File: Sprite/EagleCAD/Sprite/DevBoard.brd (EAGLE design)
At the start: 35 x 35 mm, 29 parts, among them U1 CC430F5137, U2 HMC5883LSMD, U3 ITG-3200, X1 26 MHz

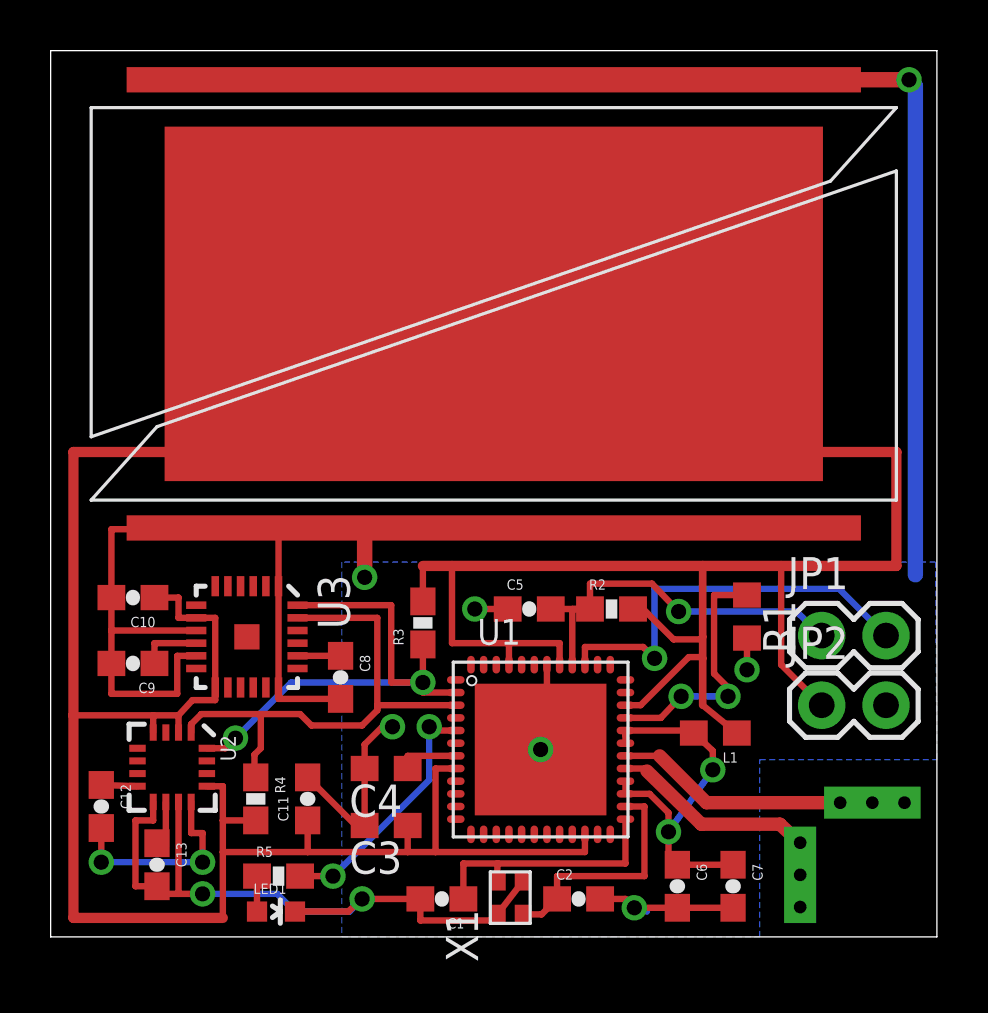
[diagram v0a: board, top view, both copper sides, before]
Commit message: Added header to dev board to disconnect solar cells
Added a header to connect/disconnect the solar cells from VCC to allow
programming with the TI launchpad
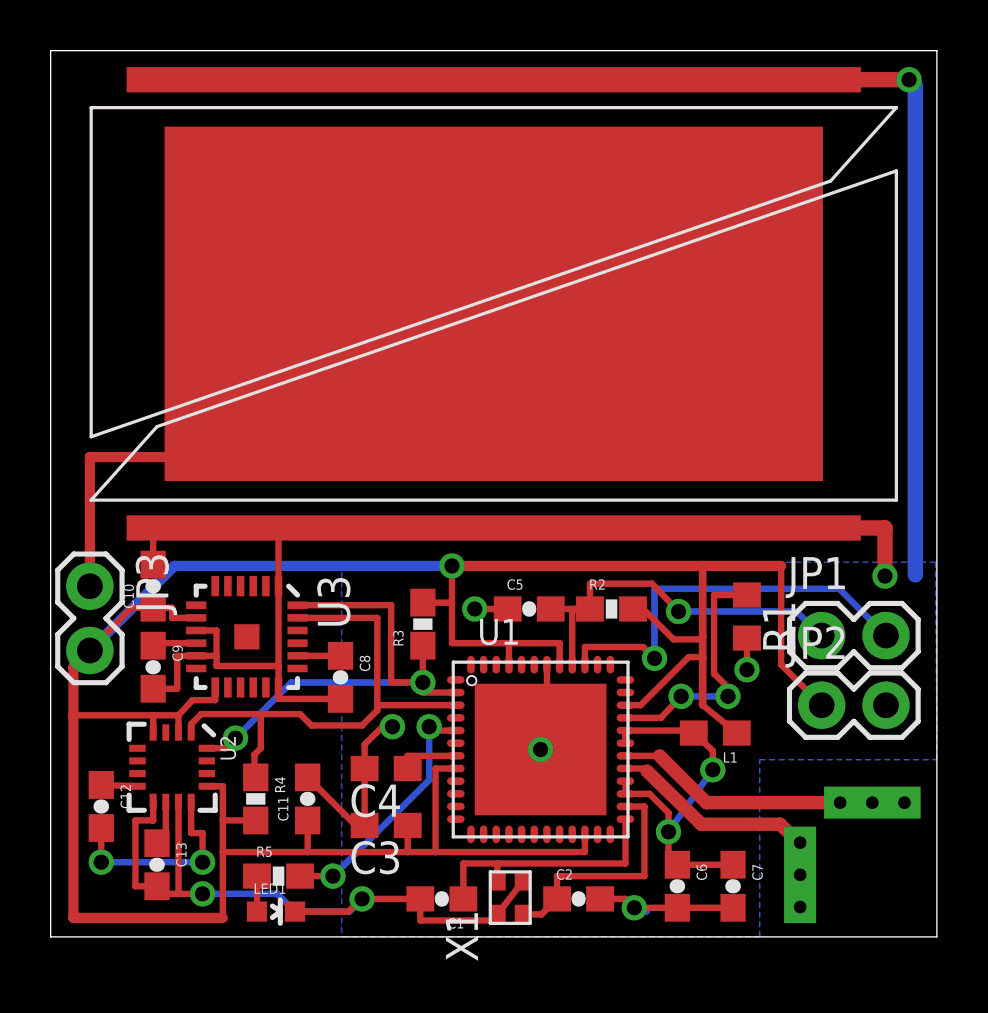
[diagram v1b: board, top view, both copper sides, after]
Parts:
- added JP3: (no value), SparkFun:1X02
- moved C10 0.92 mm to (4.05, 13.8), turned to 90 degrees
- moved C9 0.81 mm to (4.05, 10.7), turned to 270 degrees
- moved R3 0.05 mm to (14.7, 12.3)
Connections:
- new net VSOLAR: JP3.1, S1.PLUS
- net VCC: now also JP3.2; no longer S1.PLUS
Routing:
- net VCC: track 151.6 -> 117.7 mm, vias 0 -> 1
- net VSOLAR: track 0.00 -> 27.1 mm
- net GND: track 130.1 -> 156.3 mm
- net N$9: track 2.45 -> 1.76 mm
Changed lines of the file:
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@@
 <element name="U3" library="SparkFun" package="QFN-24" value="ITG-3200" x="7.75" y="11.85" rot="R270"/>
 <element name="C8" library="SparkFun" package="0603-CAP" value="2.2nF" x="11.45" y="10.25" rot="R270"/>
-<element name="C9" library="SparkFun" package="0603-CAP" value="100nF" x="3.25" y="10.8" rot="R180"/>
-<element name="C10" library="SparkFun" package="0603-CAP" value="10nF" x="3.25" y="13.4" rot="R180"/>
-<element name="R3" library="SparkFun" package="0603-RES" value="4.7K" x="14.7" y="12.4" rot="R90"/>
+<element name="C9" library="SparkFun" package="0603-CAP" value="100nF" x="4.05" y="10.65" rot="R270"/>
+<element name="C10" library="SparkFun" package="0603-CAP" value="10nF" x="4.05" y="13.85" rot="R90"/>
+<element name="R3" library="SparkFun" package="0603-RES" value="4.7K" x="14.7" y="12.35" rot="R90"/>
 <element name="R4" library="SparkFun" package="0603-RES" value="4.7K" x="8.1" y="5.45" rot="R270"/>
 <element name="JP1" library="SparkFun" package="1X02" value="" x="30.45" y="11.9"/>
@@
 <element name="R5" library="SparkFun" package="0603-RES" value="270R" x="9" y="2.4"/>
 <element name="X1" library="ABM11" package="ABM11_CERAMIC-SMD-CRYSTAL" value="26 MHz" x="18.15" y="1.55" rot="R90"/>
+<element name="JP3" library="SparkFun" package="1X02" value="" x="1.55" y="13.85" rot="R270"/>
 </elements>
 <signals>
@@
 <contactref element="R3" pad="2"/>
 <contactref element="R4" pad="2"/>
-<wire x1="33.4" y1="14.65" x2="33.4" y2="19.15" width="0.4064" layer="1"/>
-<wire x1="33.4" y1="19.15" x2="24.8" y2="19.15" width="0.4064" layer="1"/>
-<wire x1="33.4" y1="14.65" x2="28.85" y2="14.65" width="0.4064" layer="1"/>
 <wire x1="28.85" y1="14.65" x2="25.75" y2="14.65" width="0.4064" layer="1"/>
 <wire x1="25.75" y1="14.65" x2="15.85" y2="14.65" width="0.4064" layer="1"/>
-<wire x1="15.85" y1="14.65" x2="14.7" y2="14.65" width="0.4064" layer="1"/>
 <wire x1="0.9" y1="8.75" x2="0.9" y2="0.75" width="0.4064" layer="1"/>
 <wire x1="0.9" y1="0.75" x2="6.8" y2="0.75" width="0.4064" layer="1"/>
@@
 <contactref element="U3" pad="8"/>
 <contactref element="C10" pad="1"/>
-<wire x1="5.75" y1="12.6" x2="5.05" y2="12.6" width="0.254" layer="1"/>
-<wire x1="5.05" y1="12.6" x2="5.05" y2="13.4" width="0.254" layer="1"/>
-<wire x1="5.05" y1="13.4" x2="4.1" y2="13.4" width="0.254" layer="1"/>
-<wire x1="6.5" y1="9.85" x2="6.5" y2="12.6" width="0.254" layer="1"/>
-<wire x1="6.5" y1="12.6" x2="5.75" y2="12.6" width="0.254" layer="1"/>
 <wire x1="6.5" y1="9.35" x2="5.6" y2="9.35" width="0.254" layer="1"/>
 <wire x1="5.6" y1="9.35" x2="5.05" y2="8.75" width="0.254" layer="1"/>
 <contactref element="R2" pad="2"/>
-<wire x1="14.7" y1="13.25" x2="14.7" y2="14.65" width="0.254" layer="1"/>
 <contactref element="U1" pad="45"/>
 <contactref element="U1" pad="41"/>
@@
 <wire x1="18.1" y1="10.75" x2="18.1" y2="11.6" width="0.254" layer="1"/>
 <wire x1="18.1" y1="11.6" x2="15.85" y2="11.6" width="0.254" layer="1"/>
-<wire x1="15.85" y1="11.6" x2="15.85" y2="14.65" width="0.254" layer="1"/>
+<wire x1="15.85" y1="11.6" x2="15.85" y2="13.2" width="0.254" layer="1"/>
+<wire x1="15.85" y1="13.25" x2="15.85" y2="14.65" width="0.254" layer="1"/>
 <wire x1="20.1" y1="10.75" x2="20.1" y2="11.6" width="0.254" layer="1"/>
 <wire x1="20.1" y1="11.6" x2="18.1" y2="11.6" width="0.254" layer="1"/>
@@
 <wire x1="25.75" y1="11" x2="25.75" y2="9.15" width="0.3048" layer="1"/>
 <wire x1="25.75" y1="9.15" x2="27.1" y2="8.05" width="0.254" layer="1"/>
-<wire x1="0.9" y1="19.15" x2="0.9" y2="8.75" width="0.4064" layer="1"/>
 <wire x1="22.7" y1="9.15" x2="23.3" y2="9.15" width="0.254" layer="1"/>
 <wire x1="23.3" y1="9.15" x2="25.2" y2="11.05" width="0.254" layer="1"/>
@@
 <wire x1="24.6" y1="11.75" x2="25.65" y2="11.75" width="0.254" layer="1"/>
 <wire x1="25.65" y1="11.75" x2="25.75" y2="11.85" width="0.254" layer="1"/>
-<wire x1="0.9" y1="19.15" x2="17.55" y2="19.15" width="0.4064" layer="1"/>
-<wire x1="17.55" y1="19.15" x2="17.55" y2="24.85" width="0.4064" layer="1"/>
-<contactref element="S1" pad="PLUS"/>
-<wire x1="17.55" y1="24.85" x2="17.5" y2="25" width="0" layer="19" extent="1-1"/>
-<wire x1="18.1" y1="10.75" x2="16" y2="6.65" width="0" layer="19" extent="1-1"/>
+<contactref element="JP3" pad="2"/>
+<wire x1="0.9" y1="8.75" x2="0.9" y2="10.66" width="0.4064" layer="1"/>
+<wire x1="0.9" y1="10.66" x2="1.55" y2="11.31" width="0.4064" layer="1"/>
+<wire x1="5.75" y1="12.6" x2="4.8" y2="12.6" width="0.254" layer="1"/>
+<wire x1="4.8" y1="12.6" x2="4.8" y2="13" width="0.254" layer="1"/>
+<wire x1="3.2" y1="13" x2="1.55" y2="11.3" width="0.254" layer="1"/>
+<wire x1="1.55" y1="11.31" x2="1.55" y2="11.3" width="0.254" layer="1"/>
+<wire x1="4.8" y1="13" x2="4.05" y2="13" width="0.254" layer="1"/>
+<wire x1="3.2" y1="13" x2="4.05" y2="13" width="0.254" layer="1"/>
+<via x="15.85" y="14.65" extent="1-16" drill="0.6"/>
+<wire x1="15.85" y1="14.65" x2="4.89" y2="14.65" width="0.4064" layer="16"/>
+<wire x1="4.89" y1="14.65" x2="1.55" y2="11.31" width="0.4064" layer="16"/>
+<wire x1="14.7" y1="13.2" x2="15.85" y2="13.2" width="0.254" layer="1"/>
+<wire x1="15.85" y1="13.2" x2="15.85" y2="13.25" width="0.254" layer="1"/>
 </signal>
 <signal name="GND">
@@
 <vertex x="34.95" y="14.8"/>
 </polygon>
-<via x="12.4" y="14.2" extent="1-16" drill="0.6"/>
-<wire x1="12.4" y1="16.1" x2="12.4" y2="14.2" width="0.6096" layer="1"/>
+<via x="32.95" y="14.25" extent="1-16" drill="0.6"/>
 <via x="27.5" y="10.55" extent="1-16" drill="0.6"/>
 <wire x1="12.4" y1="4.4" x2="12.4" y2="6.65" width="0.254" layer="1"/>
@@
 <wire x1="4.2" y1="2" x2="4.55" y2="2.3" width="0.254" layer="1"/>
 <wire x1="5.05" y1="5.33" x2="5.05" y2="1.7" width="0.254" layer="1"/>
-<wire x1="5.75" y1="12.1" x2="2.4" y2="12.1" width="0.254" layer="1"/>
-<wire x1="2.4" y1="13.4" x2="2.4" y2="16.1" width="0.254" layer="1"/>
-<wire x1="2.4" y1="16.1" x2="12.4" y2="16.1" width="0.254" layer="1"/>
-<wire x1="2.4" y1="12.1" x2="2.4" y2="10.8" width="0.254" layer="1"/>
-<wire x1="2.4" y1="13.4" x2="2.4" y2="12.1" width="0.254" layer="1"/>
 <wire x1="9" y1="13.85" x2="9" y2="16.05" width="0.254" layer="1"/>
-<wire x1="9" y1="16.05" x2="12.4" y2="16.1" width="0.254" layer="1"/>
+<wire x1="9" y1="16.05" x2="32.95" y2="16.15" width="0.254" layer="1"/>
 <wire x1="9" y1="9.85" x2="9" y2="9.4" width="0.254" layer="1"/>
 <wire x1="9" y1="9.4" x2="11.45" y2="9.4" width="0.254" layer="1"/>
-<wire x1="9" y1="9.85" x2="9" y2="13.85" width="0.254" layer="1"/>
+<wire x1="9" y1="9.85" x2="9" y2="10.7" width="0.254" layer="1"/>
 <contactref element="JP2" pad="2"/>
+<wire x1="9" y1="10.7" x2="9" y2="13.85" width="0.254" layer="1"/>
 <wire x1="5.75" y1="11.1" x2="5" y2="11.1" width="0.254" layer="1"/>
-<wire x1="5" y1="11.1" x2="5" y2="9.6" width="0.254" layer="1"/>
-<wire x1="5" y1="9.6" x2="2.4" y2="9.6" width="0.254" layer="1"/>
-<wire x1="2.4" y1="9.6" x2="2.4" y2="10.8" width="0.254" layer="1"/>
 <contactref element="C5" pad="1"/>
 <wire x1="18.05" y1="12.95" x2="16.75" y2="12.95" width="0.254" layer="1"/>
@@
 <contactref element="S1" pad="MINUS2"/>
 <wire x1="17.5" y1="16.15" x2="12.4" y2="16.15" width="0.4064" layer="1"/>
-<wire x1="12.4" y1="16.15" x2="12.4" y2="16.1" width="0.4064" layer="1"/>
+<wire x1="17.5" y1="16.15" x2="32.95" y2="16.15" width="0.6096" layer="1"/>
 <wire x1="17.5" y1="33.85" x2="33.9" y2="33.85" width="0.6096" layer="1"/>
 <via x="33.9" y="33.85" extent="1-16" drill="0.6"/>
@@
 <wire x1="14.6" y1="0.65" x2="17.65" y2="0.65" width="0.254" layer="1"/>
 <wire x1="17.65" y1="0.65" x2="17.65" y2="0.9" width="0.254" layer="1"/>
+<wire x1="4.05" y1="9.8" x2="5" y2="9.8" width="0.254" layer="1"/>
+<wire x1="5" y1="9.8" x2="5" y2="11.1" width="0.254" layer="1"/>
+<wire x1="5.75" y1="12.1" x2="6.55" y2="12.1" width="0.254" layer="1"/>
+<wire x1="6.55" y1="12.1" x2="6.55" y2="11.1" width="0.254" layer="1"/>
+<wire x1="6.55" y1="11.1" x2="5.75" y2="11.1" width="0.254" layer="1"/>
+<wire x1="6.55" y1="11.1" x2="6.55" y2="10.7" width="0.254" layer="1"/>
+<wire x1="6.55" y1="10.7" x2="9" y2="10.7" width="0.254" layer="1"/>
+<wire x1="4.05" y1="14.7" x2="4.05" y2="16.15" width="0.254" layer="1"/>
+<wire x1="4.05" y1="16.15" x2="9" y2="16.15" width="0.254" layer="1"/>
+<wire x1="9" y1="16.15" x2="9" y2="16.05" width="0.254" layer="1"/>
+<wire x1="32.95" y1="16.15" x2="32.95" y2="14.25" width="0.6096" layer="1"/>
 </signal>
 <signal name="N$1">
@@
 <via x="7.3" y="7.85" extent="1-16" drill="0.6"/>
 <via x="14.7" y="10.05" extent="1-16" drill="0.6"/>
-<wire x1="14.7" y1="11.55" x2="14.7" y2="10.05" width="0.254" layer="1"/>
+<wire x1="14.7" y1="11.5" x2="14.7" y2="10.05" width="0.254" layer="1"/>
 <wire x1="16" y1="9.65" x2="14.7" y2="9.65" width="0.254" layer="1"/>
 <wire x1="14.7" y1="9.65" x2="14.7" y2="10.05" width="0.254" layer="1"/>
@@
 <contactref element="C9" pad="1"/>
 <wire x1="5.75" y1="11.6" x2="4.1" y2="11.6" width="0.254" layer="1"/>
-<wire x1="4.1" y1="11.6" x2="4.1" y2="10.8" width="0.254" layer="1"/>
+<wire x1="4.1" y1="11.6" x2="4.05" y2="11.5" width="0.254" layer="1"/>
 </signal>
 <signal name="VCCRF">
@@
 <wire x1="11.15" y1="2.4" x2="9.85" y2="2.4" width="0.254" layer="1"/>
 </signal>
+<signal name="VSOLAR">
+<contactref element="JP3" pad="1"/>
+<contactref element="S1" pad="PLUS"/>
+<wire x1="1.55" y1="13.85" x2="1.55" y2="18.95" width="0.4064" layer="1"/>
+<wire x1="1.55" y1="18.95" x2="17.5" y2="18.95" width="0.4064" layer="1"/>
+<wire x1="17.5" y1="18.95" x2="17.5" y2="25" width="0.4064" layer="1"/>
+</signal>
 </signals>
+<errors>
+</errors>
 </board>
 </drawing>
